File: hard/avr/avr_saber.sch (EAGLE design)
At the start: 37 parts, among them IC2 MEGA8-AI, IC6 MCP4921

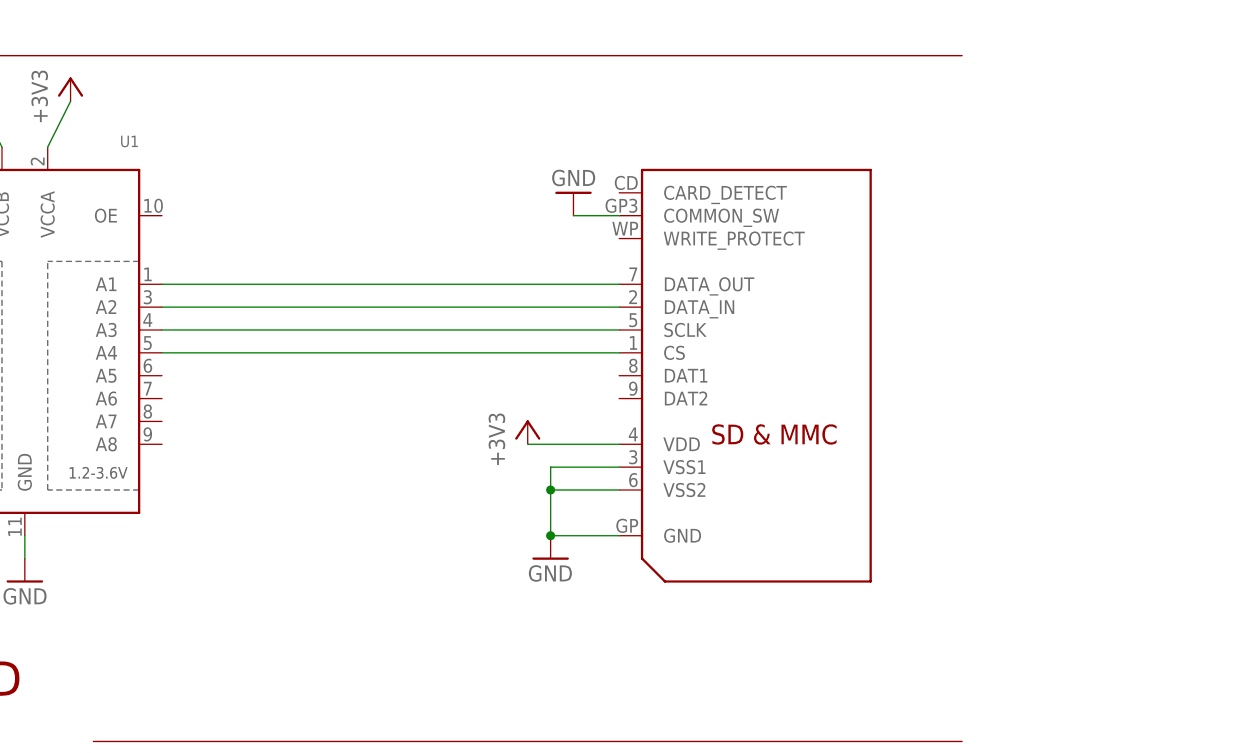
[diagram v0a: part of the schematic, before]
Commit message: Ajout microSD
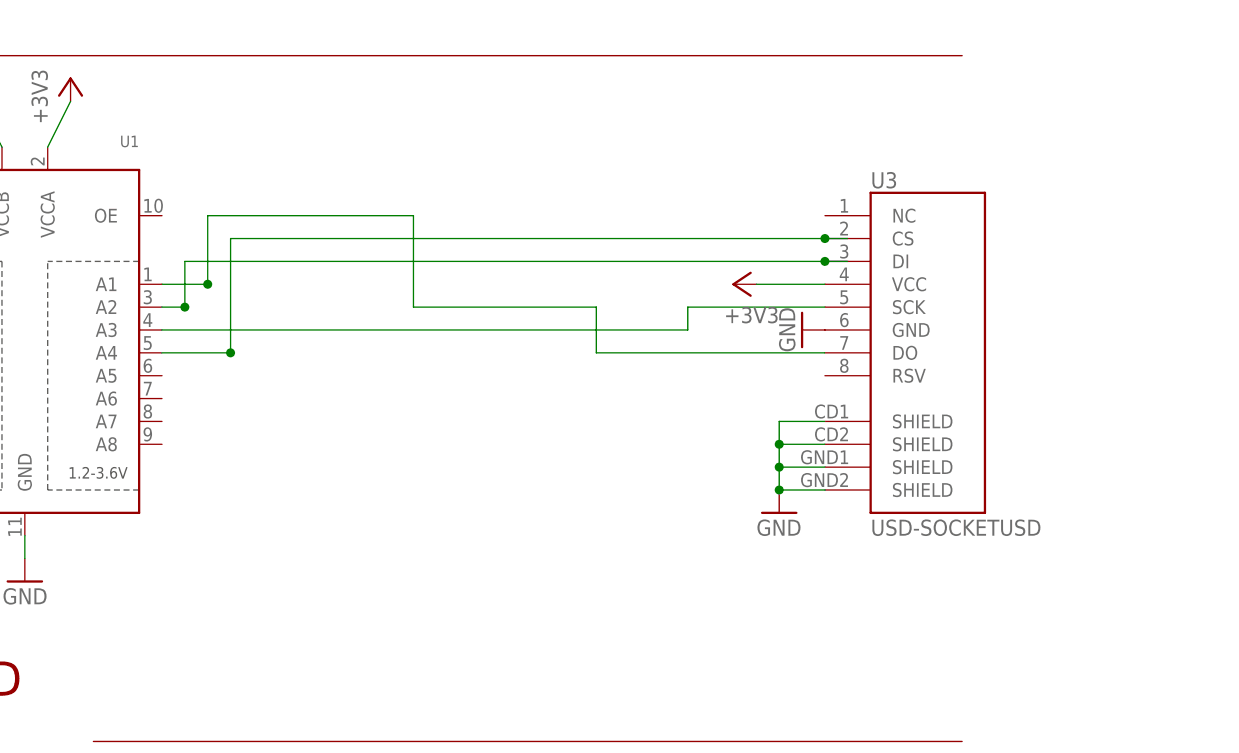
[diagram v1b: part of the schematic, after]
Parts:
- removed U$2: SDMMC06132, adafruit:SDMMC06132
- added U3: USD-SOCKETUSD, SparkFun-Connectors:USD-SOCKETUSD
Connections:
- net +3V3: now also U3.VCC; no longer U$2.VDD
- net GND: now also U3.GND, U3.SHIELD@1, U3.SHIELD@2, U3.SHIELD@3, U3.SHIELD@4; no longer U$2.COMMON_SW, U$2.GND, U$2.VSS1, U$2.VSS2
- net N$11: now also U3.DI; no longer U$2.DATA_IN
- net N$6: now also U3.SCK; no longer U$2.SCLK
- net N$7: now also U3.DO; no longer U$2.DATA_OUT
- net N$9: now also U3.CS; no longer U$2.CS
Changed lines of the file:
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@@
 <parts>
 <part name="FRAME1" library="frames" deviceset="LETTER_L" device=""/>
-<part name="U$2" library="adafruit" deviceset="SDMMC" device="06132"/>
-<part name="+3V4" library="supply1" deviceset="+3V3" device=""/>
-<part name="GND12" library="supply1" deviceset="GND" device=""/>
-<part name="GND13" library="supply1" deviceset="GND" device=""/>
 <part name="P+6" library="supply1" deviceset="+5V" device=""/>
 <part name="P+11" library="supply1" deviceset="+5V" device=""/>
@@
 <part name="C1" library="adafruit" deviceset="C-US" device="C0805" value="22p"/>
 <part name="C2" library="adafruit" deviceset="C-US" device="C0805" value="22p"/>
+<part name="U3" library="SparkFun-Connectors" deviceset="USD-SOCKET" device="USD"/>
+<part name="+3V5" library="supply1" deviceset="+3V3" device=""/>
+<part name="GND17" library="supply1" deviceset="GND" device=""/>
+<part name="GND20" library="supply1" deviceset="GND" device=""/>
 </parts>
 <sheets>
@@
 <instances>
 <instance part="FRAME1" gate="G$2" x="154.94" y="-10.16"/>
-<instance part="U$2" gate="G$1" x="231.14" y="73.66"/>
-<instance part="+3V4" gate="G$1" x="208.28" y="68.58"/>
-<instance part="GND12" gate="1" x="210.82" y="53.34"/>
-<instance part="GND13" gate="1" x="213.36" y="93.98" rot="R180"/>
 <instance part="P+6" gate="1" x="124.46" y="167.64" rot="MR0"/>
 <instance part="P+11" gate="1" x="152.4" y="152.4" rot="MR90"/>
@@
 <instance part="C1" gate="G$1" x="30.48" y="147.32" rot="R180"/>
 <instance part="C2" gate="G$1" x="-20.32" y="147.32" rot="R180"/>
+<instance part="U3" gate="G$1" x="248.92" y="78.74"/>
+<instance part="+3V5" gate="G$1" x="231.14" y="83.82" rot="R90"/>
+<instance part="GND17" gate="1" x="238.76" y="78.74" rot="R270"/>
+<instance part="GND20" gate="1" x="236.22" y="58.42"/>
 </instances>
 <busses>
@@
 </net>
 <net name="GND" class="0">
-<segment>
-<wire x1="218.44" y1="63.5" x2="210.82" y2="63.5" width="0.1524" layer="91"/>
-<wire x1="210.82" y1="63.5" x2="210.82" y2="60.96" width="0.1524" layer="91"/>
-<wire x1="210.82" y1="60.96" x2="218.44" y2="60.96" width="0.1524" layer="91"/>
-<wire x1="218.44" y1="55.88" x2="210.82" y2="55.88" width="0.1524" layer="91"/>
-<wire x1="210.82" y1="55.88" x2="210.82" y2="60.96" width="0.1524" layer="91"/>
-<junction x="210.82" y="60.96"/>
-<junction x="210.82" y="55.88"/>
-<pinref part="U$2" gate="G$1" pin="VSS1"/>
-<pinref part="U$2" gate="G$1" pin="VSS2"/>
-<pinref part="U$2" gate="G$1" pin="GND"/>
-<pinref part="GND12" gate="1" pin="GND"/>
-</segment>
-<segment>
-<wire x1="213.36" y1="91.44" x2="218.44" y2="91.44" width="0.1524" layer="91"/>
-<pinref part="U$2" gate="G$1" pin="COMMON_SW"/>
-<pinref part="GND13" gate="1" pin="GND"/>
-</segment>
 <segment>
 <wire x1="139.7" y1="157.48" x2="139.7" y2="160.02" width="0.1524" layer="91"/>
@@
 <pinref part="C2" gate="G$1" pin="1"/>
 </segment>
+<segment>
+<pinref part="U3" gate="G$1" pin="GND"/>
+<pinref part="GND17" gate="1" pin="GND"/>
+</segment>
+<segment>
+<pinref part="U3" gate="G$1" pin="SHIELD@1"/>
+<wire x1="241.3" y1="68.58" x2="236.22" y2="68.58" width="0.1524" layer="91"/>
+<wire x1="236.22" y1="68.58" x2="236.22" y2="66.04" width="0.1524" layer="91"/>
+<pinref part="U3" gate="G$1" pin="SHIELD@4"/>
+<wire x1="236.22" y1="66.04" x2="236.22" y2="63.5" width="0.1524" layer="91"/>
+<wire x1="236.22" y1="63.5" x2="236.22" y2="60.96" width="0.1524" layer="91"/>
+<wire x1="236.22" y1="60.96" x2="241.3" y2="60.96" width="0.1524" layer="91"/>
+<pinref part="U3" gate="G$1" pin="SHIELD@3"/>
+<wire x1="241.3" y1="63.5" x2="236.22" y2="63.5" width="0.1524" layer="91"/>
+<pinref part="U3" gate="G$1" pin="SHIELD@2"/>
+<wire x1="241.3" y1="66.04" x2="236.22" y2="66.04" width="0.1524" layer="91"/>
+<pinref part="GND20" gate="1" pin="GND"/>
+<junction x="236.22" y="60.96"/>
+<junction x="236.22" y="63.5"/>
+<junction x="236.22" y="66.04"/>
+</segment>
 </net>
 <net name="+3V3" class="0">
-<segment>
-<wire x1="208.28" y1="66.04" x2="218.44" y2="66.04" width="0.1524" layer="91"/>
-<pinref part="U$2" gate="G$1" pin="VDD"/>
-<pinref part="+3V4" gate="G$1" pin="+3V3"/>
-</segment>
 <segment>
 <pinref part="U1" gate="G$1" pin="VCCA"/>
@@
 <wire x1="-96.52" y1="2.54" x2="-104.14" y2="2.54" width="0.1524" layer="91"/>
 <junction x="-96.52" y="2.54"/>
+</segment>
+<segment>
+<pinref part="U3" gate="G$1" pin="VCC"/>
+<wire x1="241.3" y1="83.82" x2="233.68" y2="83.82" width="0.1524" layer="91"/>
+<pinref part="+3V5" gate="G$1" pin="+3V3"/>
 </segment>
 </net>
@@
 <net name="N$11" class="0">
 <segment>
-<pinref part="U$2" gate="G$1" pin="DATA_IN"/>
 <pinref part="U1" gate="G$1" pin="A2"/>
-<wire x1="167.64" y1="81.28" x2="218.44" y2="81.28" width="0.1524" layer="91"/>
+<wire x1="167.64" y1="81.28" x2="170.18" y2="81.28" width="0.1524" layer="91"/>
+<wire x1="243.84" y1="86.36" x2="241.3" y2="86.36" width="0.1524" layer="91"/>
+<wire x1="241.3" y1="86.36" x2="170.18" y2="86.36" width="0.1524" layer="91"/>
+<wire x1="170.18" y1="86.36" x2="170.18" y2="81.28" width="0.1524" layer="91"/>
+<junction x="170.18" y="81.28"/>
+<pinref part="U3" gate="G$1" pin="DI"/>
+<junction x="241.3" y="86.36"/>
 </segment>
 </net>
@@
 </segment>
 </net>
-<net name="N$6" class="0">
-<segment>
-<pinref part="U1" gate="G$1" pin="A3"/>
-<pinref part="U$2" gate="G$1" pin="SCLK"/>
-<wire x1="167.64" y1="78.74" x2="218.44" y2="78.74" width="0.1524" layer="91"/>
-</segment>
-</net>
 <net name="SCL" class="0">
 <segment>
@@
 <segment>
 <pinref part="U1" gate="G$1" pin="A1"/>
-<pinref part="U$2" gate="G$1" pin="DATA_OUT"/>
-<wire x1="167.64" y1="83.82" x2="218.44" y2="83.82" width="0.1524" layer="91"/>
+<wire x1="167.64" y1="83.82" x2="172.72" y2="83.82" width="0.1524" layer="91"/>
+<pinref part="U3" gate="G$1" pin="DO"/>
+<wire x1="241.3" y1="76.2" x2="215.9" y2="76.2" width="0.1524" layer="91"/>
+<wire x1="215.9" y1="76.2" x2="215.9" y2="81.28" width="0.1524" layer="91"/>
+<wire x1="215.9" y1="81.28" x2="195.58" y2="81.28" width="0.1524" layer="91"/>
+<wire x1="195.58" y1="81.28" x2="195.58" y2="91.44" width="0.1524" layer="91"/>
+<wire x1="195.58" y1="91.44" x2="172.72" y2="91.44" width="0.1524" layer="91"/>
+<wire x1="172.72" y1="91.44" x2="172.72" y2="83.82" width="0.1524" layer="91"/>
+<junction x="172.72" y="83.82"/>
 </segment>
 </net>
@@
 <segment>
 <pinref part="U1" gate="G$1" pin="A4"/>
-<pinref part="U$2" gate="G$1" pin="CS"/>
-<wire x1="167.64" y1="76.2" x2="218.44" y2="76.2" width="0.1524" layer="91"/>
-</segment>
-</net>
+<wire x1="243.84" y1="88.9" x2="241.3" y2="88.9" width="0.1524" layer="91"/>
+<wire x1="241.3" y1="88.9" x2="175.26" y2="88.9" width="0.1524" layer="91"/>
+<wire x1="175.26" y1="88.9" x2="175.26" y2="76.2" width="0.1524" layer="91"/>
+<wire x1="175.26" y1="76.2" x2="167.64" y2="76.2" width="0.1524" layer="91"/>
+<junction x="175.26" y="76.2"/>
+<pinref part="U3" gate="G$1" pin="CS"/>
+<junction x="241.3" y="88.9"/>
+</segment>
+</net>
+<net name="N$6" class="0">
+<segment>
+<pinref part="U1" gate="G$1" pin="A3"/>
+<wire x1="167.64" y1="78.74" x2="226.06" y2="78.74" width="0.1524" layer="91"/>
+<wire x1="226.06" y1="78.74" x2="226.06" y2="81.28" width="0.1524" layer="91"/>
+<pinref part="U3" gate="G$1" pin="SCK"/>
+<wire x1="226.06" y1="81.28" x2="241.3" y2="81.28" width="0.1524" layer="91"/>
+</segment>
+</net>

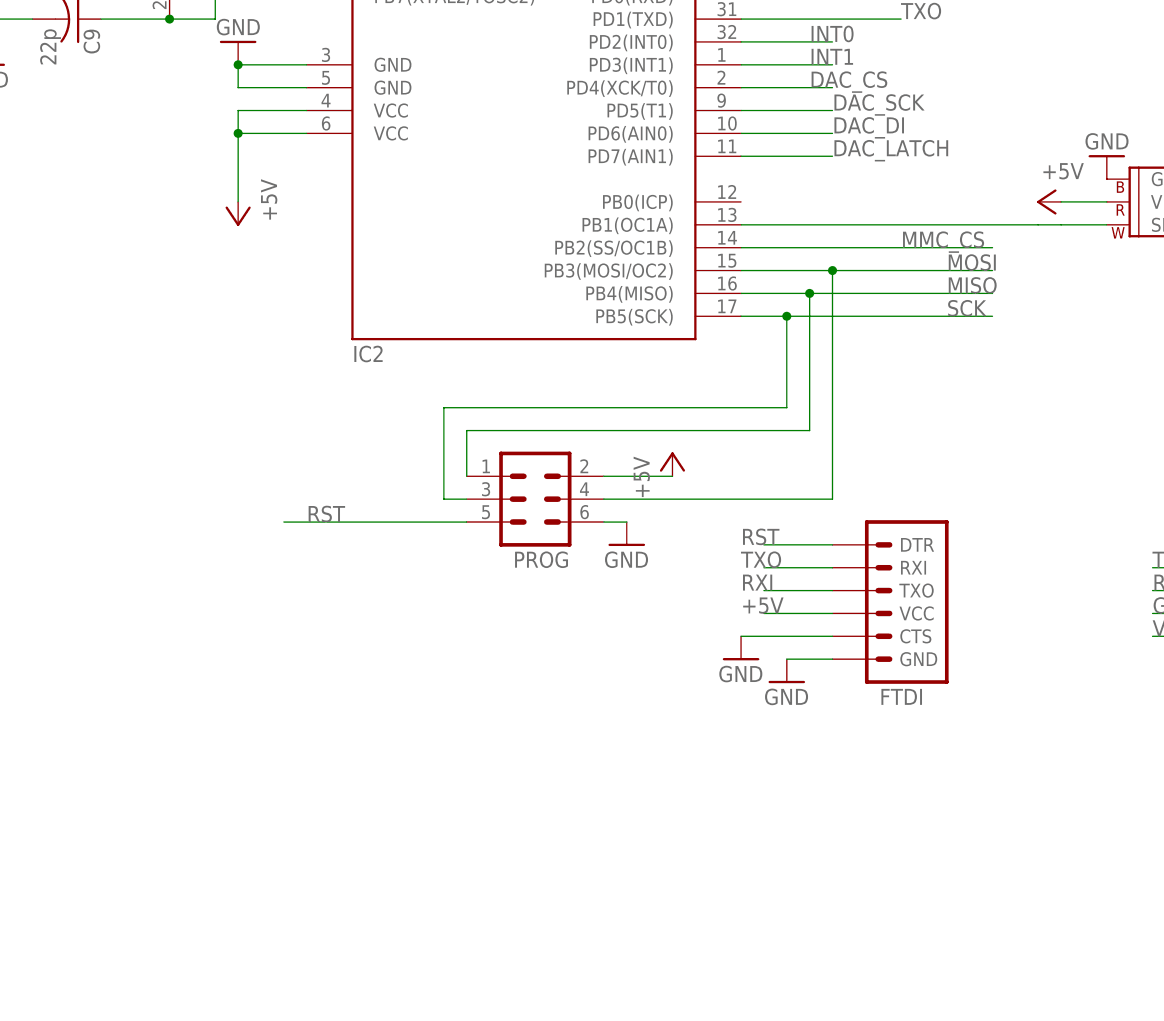
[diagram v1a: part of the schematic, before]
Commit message: ajout leds
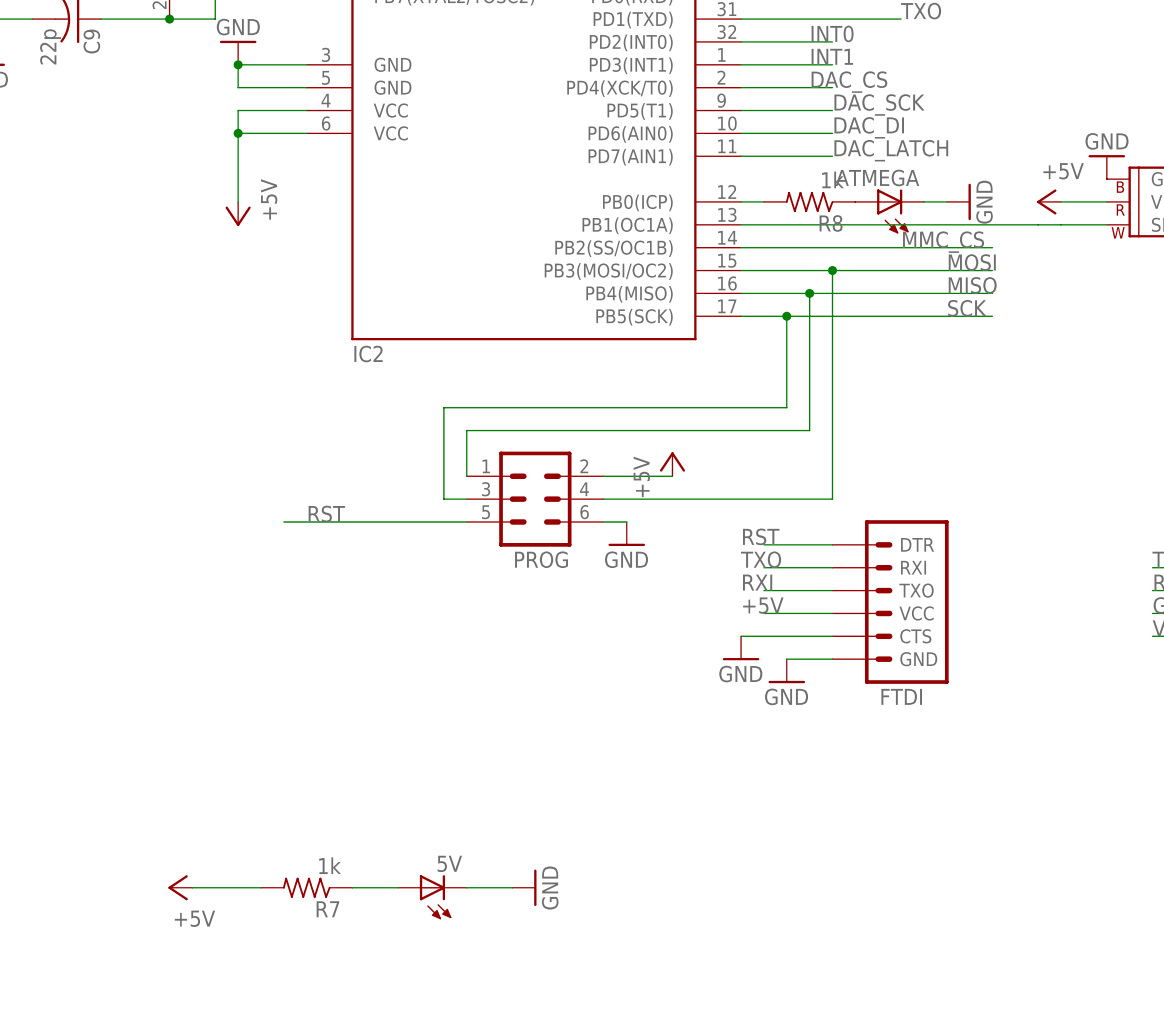
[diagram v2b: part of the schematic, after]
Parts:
- added 5V, ATMEGA: (no value), led:LEDSML0805
- added R7, R8: 1k, rcl:R-US_M0805
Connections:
- new net N$10: 5V.A, R7.1
- new net N$12: ATMEGA.A, R8.1
- new net VCC2: R8.2
- net +5V: now also R7.2
- net GND: now also 5V.C, ATMEGA.C
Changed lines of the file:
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@@
 <setting verticaltext="up"/>
 </settings>
-<grid distance="0.1" unitdist="inch" unit="inch" style="lines" multiple="1" display="yes" altdistance="0.01" altunitdist="inch" altunit="inch"/>
+<grid distance="0.1" unitdist="inch" unit="inch" style="lines" multiple="1" display="no" altdistance="0.01" altunitdist="inch" altunit="inch"/>
 <layers>
 <layer number="1" name="Top" color="4" fill="1" visible="no" active="no"/>
@@
 <part name="GND17" library="supply1" deviceset="GND" device=""/>
 <part name="GND20" library="supply1" deviceset="GND" device=""/>
+<part name="R7" library="rcl" deviceset="R-US_" device="M0805" value="1k"/>
+<part name="GND12" library="supply1" deviceset="GND" device=""/>
+<part name="5V" library="led" deviceset="LED" device="SML0805"/>
+<part name="P+13" library="supply1" deviceset="+5V" device=""/>
+<part name="R8" library="rcl" deviceset="R-US_" device="M0805" value="1k"/>
+<part name="GND13" library="supply1" deviceset="GND" device=""/>
+<part name="ATMEGA" library="led" deviceset="LED" device="SML0805"/>
 </parts>
 <sheets>
@@
 <instance part="GND17" gate="1" x="238.76" y="78.74" rot="R270"/>
 <instance part="GND20" gate="1" x="236.22" y="58.42"/>
+<instance part="R7" gate="G$1" x="-12.7" y="-27.94" rot="R180"/>
+<instance part="GND12" gate="1" x="12.7" y="-27.94" rot="R90"/>
+<instance part="5V" gate="G$1" x="0" y="-27.94" rot="R90"/>
+<instance part="P+13" gate="1" x="-27.94" y="-27.94" rot="R90"/>
+<instance part="R8" gate="G$1" x="43.18" y="48.26" rot="R180"/>
+<instance part="GND13" gate="1" x="60.96" y="48.26" rot="R90"/>
+<instance part="ATMEGA" gate="G$1" x="50.8" y="48.26" rot="R90"/>
 </instances>
 <busses>
@@
 <pinref part="P+12" gate="1" pin="+5V"/>
 <wire x1="-88.9" y1="175.26" x2="-81.28" y2="175.26" width="0.1524" layer="91"/>
+</segment>
+<segment>
+<pinref part="R7" gate="G$1" pin="2"/>
+<wire x1="-17.78" y1="-27.94" x2="-25.4" y2="-27.94" width="0.1524" layer="91"/>
+<pinref part="P+13" gate="1" pin="+5V"/>
 </segment>
 </net>
@@
 <junction x="236.22" y="66.04"/>
 </segment>
+<segment>
+<pinref part="5V" gate="G$1" pin="C"/>
+<pinref part="GND12" gate="1" pin="GND"/>
+<wire x1="5.08" y1="-27.94" x2="10.16" y2="-27.94" width="0.1524" layer="91"/>
+</segment>
+<segment>
+<pinref part="ATMEGA" gate="G$1" pin="C"/>
+<pinref part="GND13" gate="1" pin="GND"/>
+<wire x1="55.88" y1="48.26" x2="58.42" y2="48.26" width="0.1524" layer="91"/>
+</segment>
 </net>
 <net name="+3V3" class="0">
@@
 </segment>
 </net>
+<net name="N$10" class="0">
+<segment>
+<pinref part="R7" gate="G$1" pin="1"/>
+<pinref part="5V" gate="G$1" pin="A"/>
+<wire x1="-7.62" y1="-27.94" x2="-2.54" y2="-27.94" width="0.1524" layer="91"/>
+</segment>
+</net>
+<net name="VCC2" class="0">
+<segment>
+<pinref part="R8" gate="G$1" pin="2"/>
+<wire x1="38.1" y1="48.26" x2="35.56" y2="48.26" width="0.1524" layer="91"/>
+</segment>
+</net>
+<net name="N$12" class="0">
+<segment>
+<pinref part="R8" gate="G$1" pin="1"/>
+<pinref part="ATMEGA" gate="G$1" pin="A"/>
+</segment>
+</net>
